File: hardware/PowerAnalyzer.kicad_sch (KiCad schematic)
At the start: 68 parts, among them J1 EXPANSION, J10 TEST_IN, J11 PWR_IN, J12 PWR_OUT, J2 UDPI, J3 I2C, J4 FAN_OUT, J5 NTC, J6 UART, J7 USB_C_Receptacle_USB2.0_16P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

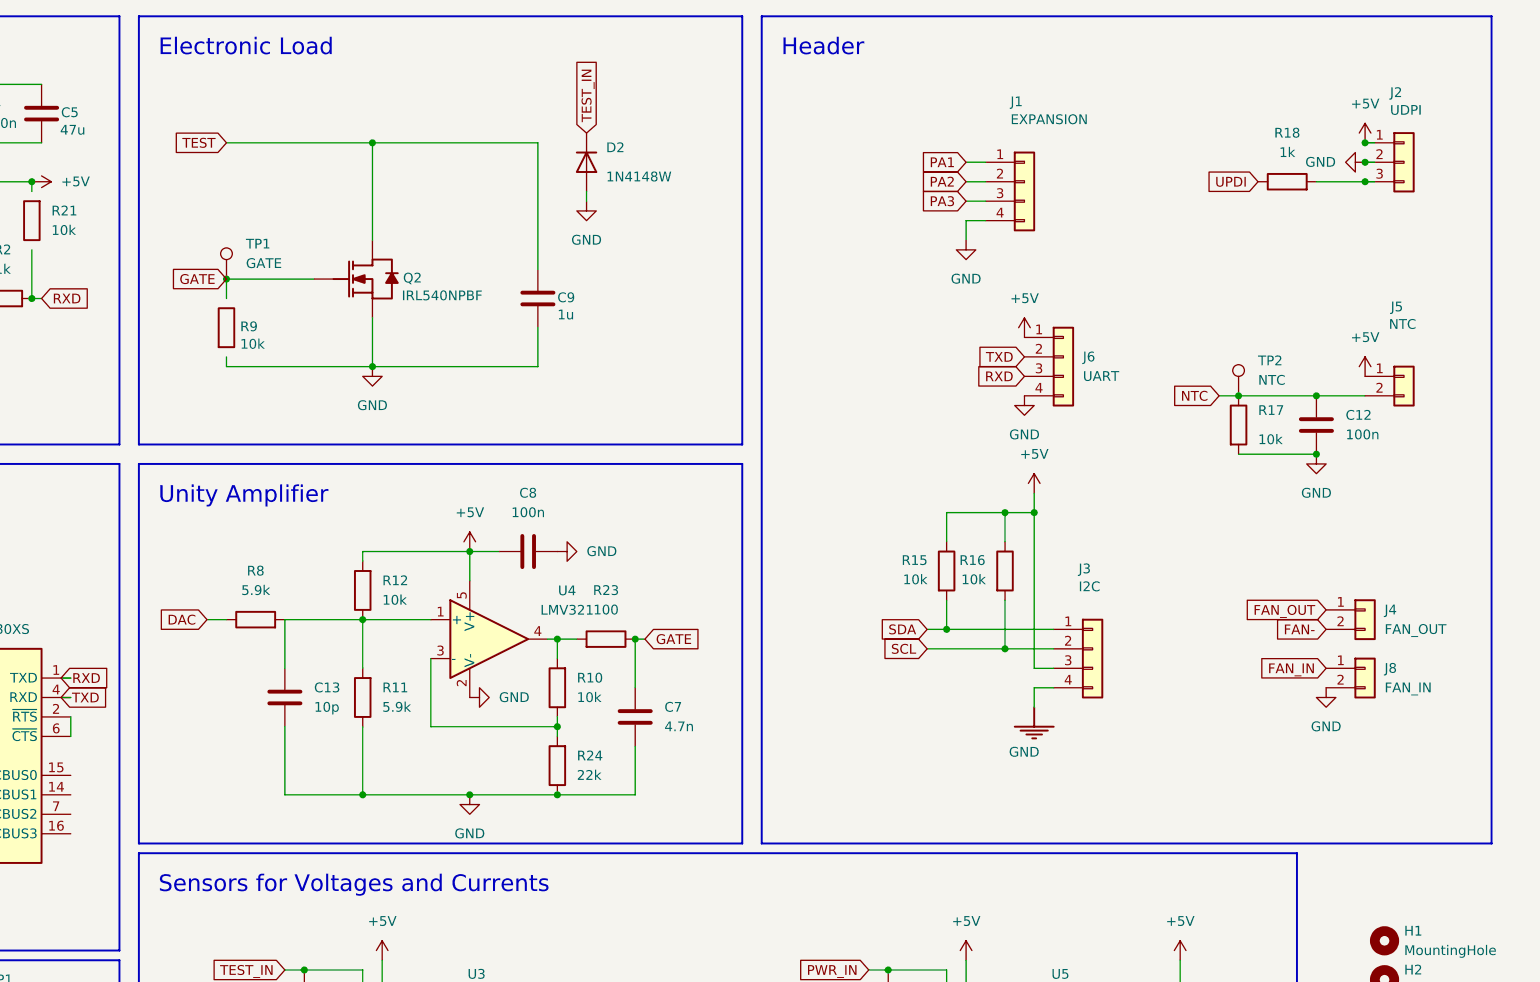
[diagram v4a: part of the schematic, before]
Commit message: More documentation in the schematic
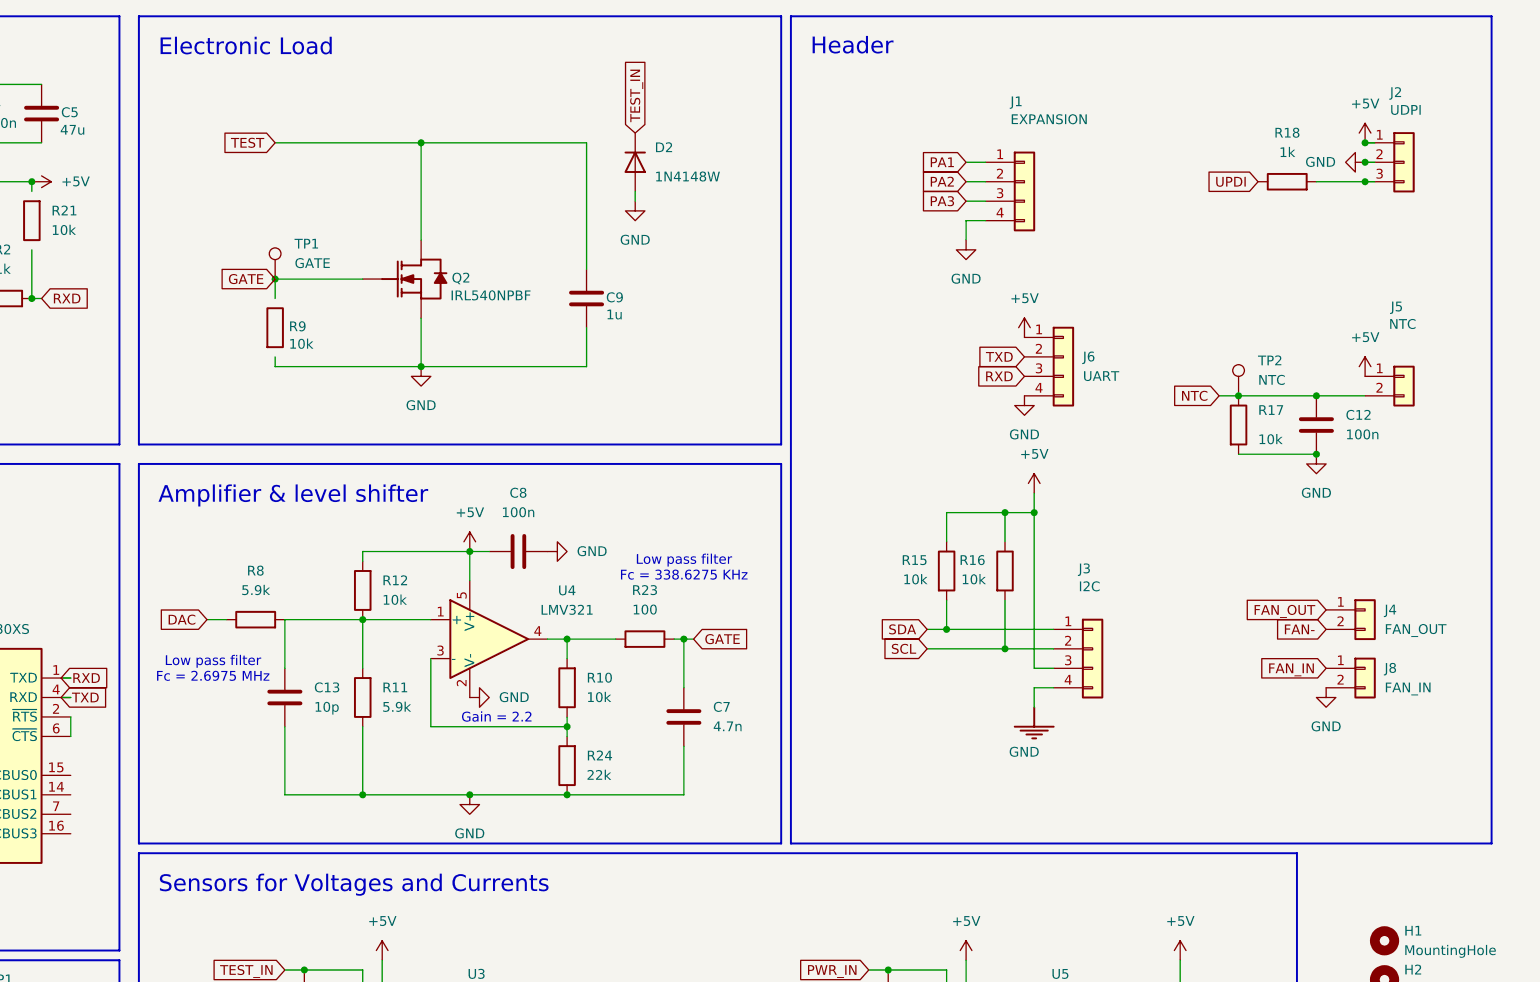
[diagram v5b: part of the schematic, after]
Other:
- note added: "Amplifier & level shifter"
- note added: "Gain = 2.2"
- note added: "Low pass filter Fc = 2.6975 MHz"
- note added: "Low pass filter Fc = 338.6275 KHz"
- note removed: "Unity Amplifier"
- moved on the sheet: C7, C8, C9, D2, Q2, R10, R23, R24, R9, TP1
